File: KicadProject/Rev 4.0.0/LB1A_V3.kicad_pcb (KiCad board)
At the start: 6 copper layers, 42 x 42 mm, 187 parts, among them J601 2337019-1, J602 2337019-1, U101 STM32MP157CAA3, U201 AS4C256M16D3LC-12BCN, U401 STPMIC1xPQR, U501 S40FC004C1B2C00000, U601 LBEE59B1LV-278, U701 DF40C-70DP-0.4V(51), U702 DF40C-100DP-0.4V(51), U703 DF40C-100DP-0.4V(51), X101 32.768kHz, Y101 24MHz

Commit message: one trace left
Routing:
- net /MPU_DDR3L_Memory/DDR_DQ8: track 0.90 -> 6.21 mm, vias 1 -> 2
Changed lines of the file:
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@@
     (thickness 1.2)
     (drawings 8)
-    (tracks 1909)
+    (tracks 1913)
     (zones 0)
     (modules 187)
@@
   (via (at 199.1 106.5) (size 0.4) (drill 0.2) (layers L1_Sig_Pwr.Cu L6_Sig_Pwr.Cu) (net 210))
   (segment (start 199.1 107.400001) (end 199.1 106.5) (width 0.127) (layer L1_Sig_Pwr.Cu) (net 210))
+  (via (at 198 97.7) (size 0.4) (drill 0.2) (layers L1_Sig_Pwr.Cu L6_Sig_Pwr.Cu) (net 210))
+  (segment (start 197.931499 97.768501) (end 198 97.7) (width 0.127) (layer L1_Sig_Pwr.Cu) (net 210))
+  (segment (start 197.023119 97.768501) (end 197.931499 97.768501) (width 0.127) (layer L1_Sig_Pwr.Cu) (net 210))
+  (segment (start 196.831499 96.486117) (end 196.831499 97.576881) (width 0.127) (layer L1_Sig_Pwr.Cu) (net 210))
+  (segment (start 196.576881 96.231499) (end 196.831499 96.486117) (width 0.127) (layer L1_Sig_Pwr.Cu) (net 210))
+  (segment (start 196.286117 96.231499) (end 196.576881 96.231499) (width 0.127) (layer L1_Sig_Pwr.Cu) (net 210))
+  (segment (start 196.831499 97.576881) (end 197.023119 97.768501) (width 0.127) (layer L1_Sig_Pwr.Cu) (net 210))
+  (segment (start 196.031499 95.976881) (end 196.286117 96.231499) (width 0.127) (layer L1_Sig_Pwr.Cu) (net 210))
+  (segment (start 196.031499 94.568501) (end 196.031499 95.976881) (width 0.127) (layer L1_Sig_Pwr.Cu) (net 210))
+  (segment (start 196.4 94.2) (end 196.031499 94.568501) (width 0.127) (layer L1_Sig_Pwr.Cu) (net 210))
   (segment (start 196.831499 95.976881) (end 197.086117 96.231499) (width 0.127) (layer L1_Sig_Pwr.Cu) (net 212))
   (segment (start 196.4 95) (end 196.4 95.2) (width 0.127) (layer L1_Sig_Pwr.Cu) (net 212))
@@
   (segment (start 197.968501 96.231499) (end 198 96.2) (width 0.127) (layer L1_Sig_Pwr.Cu) (net 212))
   (segment (start 197.086117 96.231499) (end 197.968501 96.231499) (width 0.127) (layer L1_Sig_Pwr.Cu) (net 212))
-  (segment (start 200.036499 97.063501) (end 200.036499 105.463501) (width 0.127) (layer L3_Sig_Pwr.Cu) (net 212))
-  (segment (start 200.1 97) (end 200.036499 97.063501) (width 0.127) (layer L3_Sig_Pwr.Cu) (net 212))
-  (segment (start 200.1 92.9) (end 200.1 97) (width 0.127) (layer L3_Sig_Pwr.Cu) (net 212))
-  (segment (start 200 92.8) (end 200.1 92.9) (width 0.127) (layer L3_Sig_Pwr.Cu) (net 212))
-  (segment (start 199.7 105.8) (end 199.1 105.8) (width 0.127) (layer L3_Sig_Pwr.Cu) (net 212))
-  (segment (start 199.8 92.8) (end 200 92.8) (width 0.127) (layer L3_Sig_Pwr.Cu) (net 212))
-  (segment (start 199.7 96.1) (end 199.7 92.9) (width 0.127) (layer L3_Sig_Pwr.Cu) (net 212))
-  (segment (start 199.3 96.1) (end 199.4 96.2) (width 0.127) (layer L3_Sig_Pwr.Cu) (net 212))
-  (segment (start 198 96.2) (end 198.1 96.1) (width 0.127) (layer L3_Sig_Pwr.Cu) (net 212))
-  (segment (start 199.7 92.9) (end 199.8 92.8) (width 0.127) (layer L3_Sig_Pwr.Cu) (net 212))
-  (segment (start 198.1 92.9) (end 198.2 92.8) (width 0.127) (layer L3_Sig_Pwr.Cu) (net 212))
-  (segment (start 199.3 92.9) (end 199.3 96.1) (width 0.127) (layer L3_Sig_Pwr.Cu) (net 212))
-  (segment (start 198.6 96.2) (end 198.8 96.2) (width 0.127) (layer L3_Sig_Pwr.Cu) (net 212))
-  (segment (start 199.4 96.2) (end 199.6 96.2) (width 0.127) (layer L3_Sig_Pwr.Cu) (net 212))
-  (segment (start 198.2 92.8) (end 198.4 92.8) (width 0.127) (layer L3_Sig_Pwr.Cu) (net 212))
-  (segment (start 200.036499 105.463501) (end 199.7 105.8) (width 0.127) (layer L3_Sig_Pwr.Cu) (net 212))
-  (segment (start 198.4 92.8) (end 198.5 92.9) (width 0.127) (layer L3_Sig_Pwr.Cu) (net 212))
-  (segment (start 198.5 92.9) (end 198.5 96.1) (width 0.127) (layer L3_Sig_Pwr.Cu) (net 212))
-  (segment (start 198.5 96.1) (end 198.6 96.2) (width 0.127) (layer L3_Sig_Pwr.Cu) (net 212))
-  (segment (start 199.6 96.2) (end 199.7 96.1) (width 0.127) (layer L3_Sig_Pwr.Cu) (net 212))
-  (segment (start 198.1 96.1) (end 198.1 92.9) (width 0.127) (layer L3_Sig_Pwr.Cu) (net 212))
-  (segment (start 198.9 92.9) (end 199 92.8) (width 0.127) (layer L3_Sig_Pwr.Cu) (net 212))
-  (segment (start 198.8 96.2) (end 198.9 96.1) (width 0.127) (layer L3_Sig_Pwr.Cu) (net 212))
-  (segment (start 198.9 96.1) (end 198.9 92.9) (width 0.127) (layer L3_Sig_Pwr.Cu) (net 212))
-  (segment (start 199 92.8) (end 199.2 92.8) (width 0.127) (layer L3_Sig_Pwr.Cu) (net 212))
-  (segment (start 199.2 92.8) (end 199.3 92.9) (width 0.127) (layer L3_Sig_Pwr.Cu) (net 212))
   (segment (start 199.7 108.000001) (end 199.9 108.200001) (width 0.127) (layer L1_Sig_Pwr.Cu) (net 212))
   (segment (start 199.2 105.8) (end 199.3 105.7) (width 0.127) (layer L1_Sig_Pwr.Cu) (net 212))
@@
   (segment (start 199.6 104.6) (end 199.7 104.7) (width 0.127) (layer L1_Sig_Pwr.Cu) (net 212))
   (segment (start 199.7 104.7) (end 199.7 108.000001) (width 0.127) (layer L1_Sig_Pwr.Cu) (net 212))
+  (segment (start 204.572018 93) (end 204.772018 93.2) (width 0.127) (layer L3_Sig_Pwr.Cu) (net 212))
+  (segment (start 201.062018 93) (end 204.572018 93) (width 0.127) (layer L3_Sig_Pwr.Cu) (net 212))
+  (segment (start 200.862018 92.8) (end 201.062018 93) (width 0.127) (layer L3_Sig_Pwr.Cu) (net 212))
+  (segment (start 198.2 92.8) (end 200.862018 92.8) (width 0.127) (layer L3_Sig_Pwr.Cu) (net 212))
+  (segment (start 198.1 92.9) (end 198.2 92.8) (width 0.127) (layer L3_Sig_Pwr.Cu) (net 212))
+  (segment (start 198.1 96.1) (end 198.1 92.9) (width 0.127) (layer L3_Sig_Pwr.Cu) (net 212))
+  (segment (start 198 96.2) (end 198.1 96.1) (width 0.127) (layer L3_Sig_Pwr.Cu) (net 212))
+  (segment (start 202.7 93.7) (end 202.7 96.5) (width 0.127) (layer L3_Sig_Pwr.Cu) (net 212))
+  (segment (start 202.8 93.6) (end 202.7 93.7) (width 0.127) (layer L3_Sig_Pwr.Cu) (net 212))
+  (segment (start 202.7 96.5) (end 202.663501 96.536499) (width 0.127) (layer L3_Sig_Pwr.Cu) (net 212))
+  (segment (start 202.663501 96.536499) (end 200.163501 96.536499) (width 0.127) (layer L3_Sig_Pwr.Cu) (net 212))
+  (segment (start 200.163501 96.536499) (end 200.036499 96.663501) (width 0.127) (layer L3_Sig_Pwr.Cu) (net 212))
+  (segment (start 200.036499 96.663501) (end 200.036499 105.463501) (width 0.127) (layer L3_Sig_Pwr.Cu) (net 212))
+  (segment (start 200.036499 105.463501) (end 199.7 105.8) (width 0.127) (layer L3_Sig_Pwr.Cu) (net 212))
+  (segment (start 199.7 105.8) (end 199.1 105.8) (width 0.127) (layer L3_Sig_Pwr.Cu) (net 212))
+  (segment (start 206.8 93.2) (end 206.9 93.3) (width 0.127) (layer L3_Sig_Pwr.Cu) (net 212))
+  (segment (start 204.772018 93.2) (end 206.8 93.2) (width 0.127) (layer L3_Sig_Pwr.Cu) (net 212))
+  (segment (start 206.9 93.3) (end 206.9 93.5) (width 0.127) (layer L3_Sig_Pwr.Cu) (net 212))
+  (segment (start 206.9 93.5) (end 206.8 93.6) (width 0.127) (layer L3_Sig_Pwr.Cu) (net 212))
+  (segment (start 206.8 93.6) (end 202.8 93.6) (width 0.127) (layer L3_Sig_Pwr.Cu) (net 212))
   (segment (start 200.149489 107.97053) (end 200.149489 105.250511) (width 0.127) (layer L1_Sig_Pwr.Cu) (net 215))
   (segment (start 200.376499 108.19754) (end 200.149489 107.97053) (width 0.127) (layer L1_Sig_Pwr.Cu) (net 215))

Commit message: top plane all ddr3 traces completed
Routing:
- net /MPU_DDR3L_Memory/DDR_DQ8: track 6.21 -> 39.9 mm
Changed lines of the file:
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@@
     (thickness 1.2)
     (drawings 8)
-    (tracks 1913)
+    (tracks 1943)
     (zones 0)
     (modules 187)
@@
   (segment (start 196.031499 94.568501) (end 196.031499 95.976881) (width 0.127) (layer L1_Sig_Pwr.Cu) (net 210))
   (segment (start 196.4 94.2) (end 196.031499 94.568501) (width 0.127) (layer L1_Sig_Pwr.Cu) (net 210))
+  (segment (start 199.2 102.4) (end 199.2 99.2) (width 0.127) (layer L3_Sig_Pwr.Cu) (net 210))
+  (segment (start 199.3 102.5) (end 199.2 102.4) (width 0.127) (layer L3_Sig_Pwr.Cu) (net 210))
+  (segment (start 199.6 97.9) (end 199.6 102.4) (width 0.127) (layer L3_Sig_Pwr.Cu) (net 210))
+  (segment (start 198.8 99.1) (end 198.736499 99.163501) (width 0.127) (layer L3_Sig_Pwr.Cu) (net 210))
+  (segment (start 199.7 97.8) (end 199.6 97.9) (width 0.127) (layer L3_Sig_Pwr.Cu) (net 210))
+  (segment (start 199.5 102.5) (end 199.3 102.5) (width 0.127) (layer L3_Sig_Pwr.Cu) (net 210))
+  (segment (start 199.6 102.4) (end 199.5 102.5) (width 0.127) (layer L3_Sig_Pwr.Cu) (net 210))
+  (segment (start 198.5 97.6) (end 198.5 93.5) (width 0.127) (layer L3_Sig_Pwr.Cu) (net 210))
+  (segment (start 198.736499 99.163501) (end 198.736499 106.136499) (width 0.127) (layer L3_Sig_Pwr.Cu) (net 210))
+  (segment (start 198.8 93.4) (end 198.9 93.5) (width 0.127) (layer L3_Sig_Pwr.Cu) (net 210))
+  (segment (start 198 97.7) (end 198.4 97.7) (width 0.127) (layer L3_Sig_Pwr.Cu) (net 210))
+  (segment (start 199.7 93.5) (end 199.7 97.8) (width 0.127) (layer L3_Sig_Pwr.Cu) (net 210))
+  (segment (start 198.6 93.4) (end 198.8 93.4) (width 0.127) (layer L3_Sig_Pwr.Cu) (net 210))
+  (segment (start 199.1 99.1) (end 198.8 99.1) (width 0.127) (layer L3_Sig_Pwr.Cu) (net 210))
+  (segment (start 199.6 93.4) (end 199.7 93.5) (width 0.127) (layer L3_Sig_Pwr.Cu) (net 210))
+  (segment (start 198.736499 106.136499) (end 199.1 106.5) (width 0.127) (layer L3_Sig_Pwr.Cu) (net 210))
+  (segment (start 199.2 99.2) (end 199.1 99.1) (width 0.127) (layer L3_Sig_Pwr.Cu) (net 210))
+  (segment (start 198.4 97.7) (end 198.5 97.6) (width 0.127) (layer L3_Sig_Pwr.Cu) (net 210))
+  (segment (start 199.3 93.5) (end 199.4 93.4) (width 0.127) (layer L3_Sig_Pwr.Cu) (net 210))
+  (segment (start 198.5 93.5) (end 198.6 93.4) (width 0.127) (layer L3_Sig_Pwr.Cu) (net 210))
+  (segment (start 199.4 93.4) (end 199.6 93.4) (width 0.127) (layer L3_Sig_Pwr.Cu) (net 210))
+  (segment (start 198.9 97) (end 199 97.1) (width 0.127) (layer L3_Sig_Pwr.Cu) (net 210))
+  (segment (start 198.9 93.5) (end 198.9 97) (width 0.127) (layer L3_Sig_Pwr.Cu) (net 210))
+  (segment (start 199 97.1) (end 199.2 97.1) (width 0.127) (layer L3_Sig_Pwr.Cu) (net 210))
+  (segment (start 199.2 97.1) (end 199.3 97) (width 0.127) (layer L3_Sig_Pwr.Cu) (net 210))
+  (segment (start 199.3 97) (end 199.3 93.5) (width 0.127) (layer L3_Sig_Pwr.Cu) (net 210))
   (segment (start 196.831499 95.976881) (end 197.086117 96.231499) (width 0.127) (layer L1_Sig_Pwr.Cu) (net 212))
   (segment (start 196.4 95) (end 196.4 95.2) (width 0.127) (layer L1_Sig_Pwr.Cu) (net 212))
@@
   (segment (start 202.663501 96.536499) (end 200.163501 96.536499) (width 0.127) (layer L3_Sig_Pwr.Cu) (net 212))
   (segment (start 200.163501 96.536499) (end 200.036499 96.663501) (width 0.127) (layer L3_Sig_Pwr.Cu) (net 212))
-  (segment (start 200.036499 96.663501) (end 200.036499 105.463501) (width 0.127) (layer L3_Sig_Pwr.Cu) (net 212))
-  (segment (start 200.036499 105.463501) (end 199.7 105.8) (width 0.127) (layer L3_Sig_Pwr.Cu) (net 212))
-  (segment (start 199.7 105.8) (end 199.1 105.8) (width 0.127) (layer L3_Sig_Pwr.Cu) (net 212))
   (segment (start 206.8 93.2) (end 206.9 93.3) (width 0.127) (layer L3_Sig_Pwr.Cu) (net 212))
   (segment (start 204.772018 93.2) (end 206.8 93.2) (width 0.127) (layer L3_Sig_Pwr.Cu) (net 212))
@@
   (segment (start 206.9 93.5) (end 206.8 93.6) (width 0.127) (layer L3_Sig_Pwr.Cu) (net 212))
   (segment (start 206.8 93.6) (end 202.8 93.6) (width 0.127) (layer L3_Sig_Pwr.Cu) (net 212))
+  (segment (start 199.1 105.8) (end 199.1 105.7) (width 0.127) (layer L3_Sig_Pwr.Cu) (net 212))
+  (segment (start 199.1 105.7) (end 199.2 105.6) (width 0.127) (layer L3_Sig_Pwr.Cu) (net 212))
+  (segment (start 199.2 105.6) (end 199.2 103) (width 0.127) (layer L3_Sig_Pwr.Cu) (net 212))
+  (segment (start 199.2 103) (end 199.3 102.9) (width 0.127) (layer L3_Sig_Pwr.Cu) (net 212))
+  (segment (start 199.9 102.9) (end 200.036499 102.763501) (width 0.127) (layer L3_Sig_Pwr.Cu) (net 212))
+  (segment (start 199.3 102.9) (end 199.9 102.9) (width 0.127) (layer L3_Sig_Pwr.Cu) (net 212))
+  (segment (start 200.036499 96.663501) (end 200.036499 102.763501) (width 0.127) (layer L3_Sig_Pwr.Cu) (net 212))
   (segment (start 200.149489 107.97053) (end 200.149489 105.250511) (width 0.127) (layer L1_Sig_Pwr.Cu) (net 215))
   (segment (start 200.376499 108.19754) (end 200.149489 107.97053) (width 0.127) (layer L1_Sig_Pwr.Cu) (net 215))

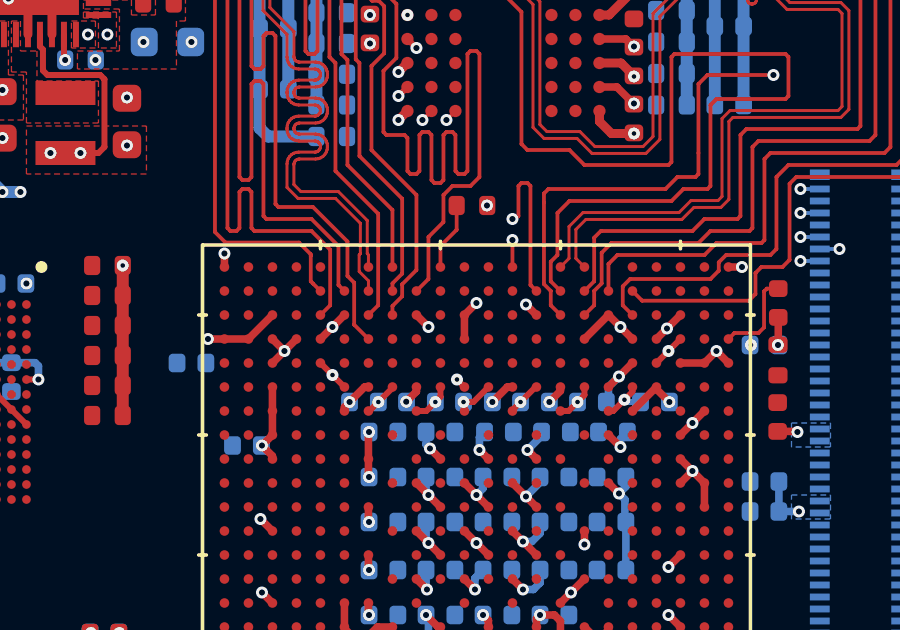
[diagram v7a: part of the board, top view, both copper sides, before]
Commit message: working on bottom layer ddr traces
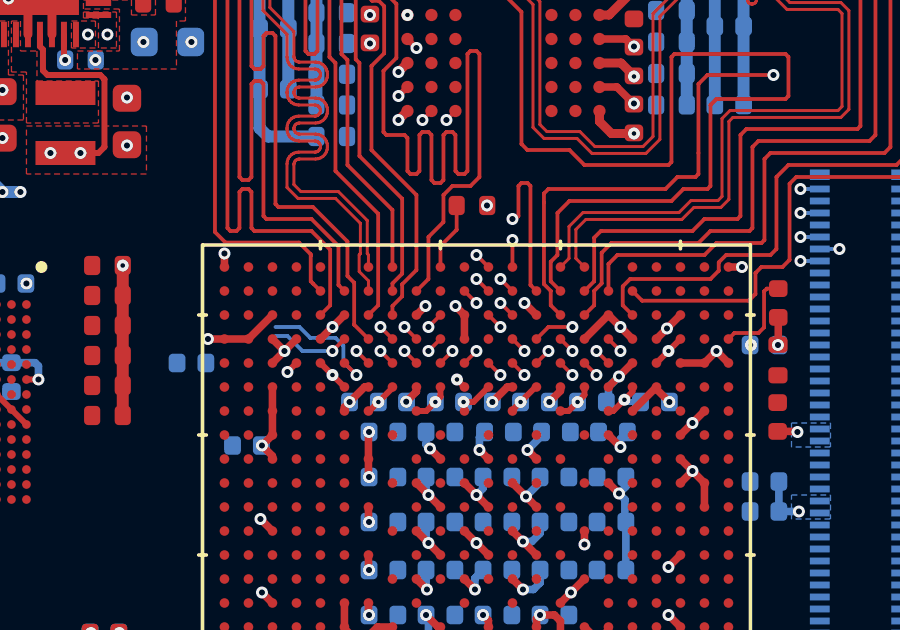
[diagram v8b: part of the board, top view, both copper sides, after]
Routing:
- net /MPU_DDR3L_Memory/DDR_A7: track 0.00 -> 4.24 mm, vias 0 -> 1
- net /MPU_DDR3L_Memory/DDR_RESETN: track 0.42 -> 3.10 mm, vias 1 -> 2
- net /MPU_DDR3L_Memory/DDR_A11: track 0.00 -> 1.37 mm, vias 0 -> 1
- net /MPU_DDR3L_Memory/DDR_CSN: track 0.00 -> 0.57 mm, vias 0 -> 1
- net /MPU_DDR3L_Memory/DDR_BA2: track 0.00 -> 0.57 mm, vias 0 -> 1
- net /MPU_DDR3L_Memory/DDR_A9: track 0.00 -> 0.57 mm, vias 0 -> 1
- net /MPU_DDR3L_Memory/DDR_A8: track 0.00 -> 0.57 mm, vias 0 -> 1
- net /MPU_DDR3L_Memory/DDR_A2: track 0.00 -> 0.57 mm, vias 0 -> 1
- net /MPU_DDR3L_Memory/DDR_A14: track 0.00 -> 0.57 mm, vias 0 -> 1
- net /MPU_DDR3L_Memory/DDR_A13: track 0.42 -> 0.99 mm, vias 1 -> 2
- net /MPU_DDR3L_Memory/DDR_WEN: track 0.00 -> 0.57 mm, vias 0 -> 1
- net /MPU_DDR3L_Memory/DDR_CLK_P: track 0.00 -> 0.57 mm, vias 0 -> 1
- net /MPU_DDR3L_Memory/DDR_CLK_N: track 0.00 -> 0.57 mm, vias 1 -> 2
- net /MPU_DDR3L_Memory/DDR_CASN: track 0.00 -> 0.57 mm, vias 0 -> 1
- net /MPU_DDR3L_Memory/DDR_A5: track 0.00 -> 0.57 mm, vias 0 -> 1
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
